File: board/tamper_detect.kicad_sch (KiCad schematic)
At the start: 12 parts

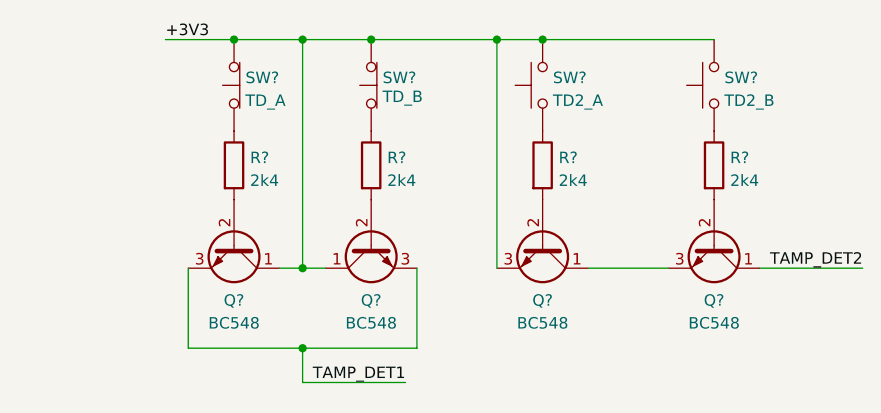
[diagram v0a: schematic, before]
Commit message: Add missing footprints.
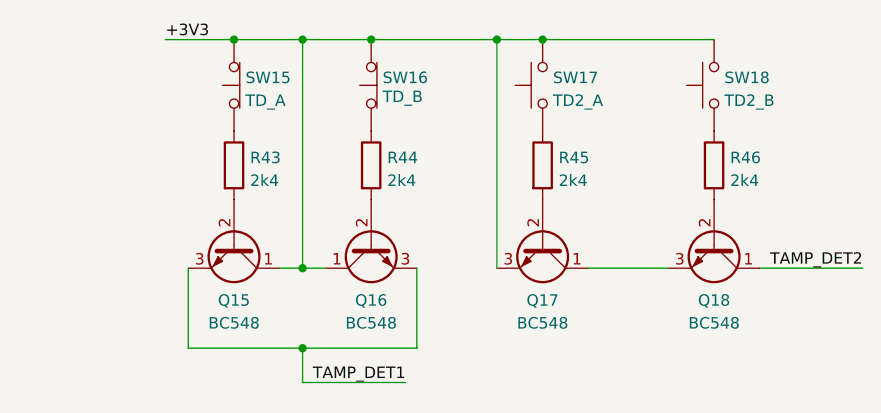
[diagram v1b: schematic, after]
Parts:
- R43, R44, R45, R46: renamed from R?; footprint (none) -> Resistor_THT:R_Axial_DIN0516_L15.5mm_D5.0mm_P7.62mm_Vertical
- SW15, SW16, SW17, SW18: renamed from SW?; footprint (none) -> Connector_Wire:SolderWire-1sqmm_1x02_P5.4mm_D1.4mm_OD2.7mm
- gave numbers to parts that had none: 4
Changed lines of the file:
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@@
   (symbol (lib_id "Device:R") (at 99.06 40.64 0) (unit 1)
     (in_bom yes) (on_board yes) (fields_autoplaced)
-    (property "Reference" "R?" (id 0) (at 100.838 39.8053 0)
+    (property "Reference" "R46" (id 0) (at 100.838 39.8053 0)
       (effects (font (size 1.27 1.27)) (justify left))
     )
@@
       (effects (font (size 1.27 1.27)) (justify left))
     )
-    (property "Footprint" "" (id 2) (at 97.282 40.64 90)
+    (property "Footprint" "Resistor_THT:R_Axial_DIN0516_L15.5mm_D5.0mm_P7.62mm_Vertical" (id 2) (at 97.282 40.64 90)
       (effects (font (size 1.27 1.27)) hide)
     )
@@
   (symbol (lib_id "Switch:SW_Push") (at 99.06 31.75 90) (unit 1)
     (in_bom yes) (on_board yes)
-    (property "Reference" "SW?" (id 0) (at 100.203 30.9153 90)
+    (property "Reference" "SW18" (id 0) (at 100.203 30.9153 90)
       (effects (font (size 1.27 1.27)) (justify right))
     )
@@
       (effects (font (size 1.27 1.27)) (justify right))
     )
-    (property "Footprint" "" (id 2) (at 93.98 31.75 0)
+    (property "Footprint" "Connector_Wire:SolderWire-1sqmm_1x02_P5.4mm_D1.4mm_OD2.7mm" (id 2) (at 93.98 31.75 0)
       (effects (font (size 1.27 1.27)) hide)
     )
@@
   (symbol (lib_id "Transistor_BJT:BC548") (at 80.01 49.53 270) (unit 1)
     (in_bom yes) (on_board yes) (fields_autoplaced)
-    (property "Reference" "Q?" (id 0) (at 80.01 55.6498 90))
+    (property "Reference" "Q17" (id 0) (at 80.01 55.6498 90))
     (property "Value" "BC548" (id 1) (at 80.01 58.1867 90))
     (property "Footprint" "Package_TO_SOT_THT:TO-92_Inline" (id 2) (at 78.105 54.61 0)
@@
   (symbol (lib_id "Device:R") (at 60.96 40.64 0) (unit 1)
     (in_bom yes) (on_board yes) (fields_autoplaced)
-    (property "Reference" "R?" (id 0) (at 62.738 39.8053 0)
+    (property "Reference" "R44" (id 0) (at 62.738 39.8053 0)
       (effects (font (size 1.27 1.27)) (justify left))
     )
@@
       (effects (font (size 1.27 1.27)) (justify left))
     )
-    (property "Footprint" "" (id 2) (at 59.182 40.64 90)
+    (property "Footprint" "Resistor_THT:R_Axial_DIN0516_L15.5mm_D5.0mm_P7.62mm_Vertical" (id 2) (at 59.182 40.64 90)
       (effects (font (size 1.27 1.27)) hide)
     )
@@
   (symbol (lib_id "Switch:SW_Push_Open") (at 45.72 31.75 90) (unit 1)
     (in_bom yes) (on_board yes) (fields_autoplaced)
-    (property "Reference" "SW?" (id 0) (at 46.99 30.9153 90)
+    (property "Reference" "SW15" (id 0) (at 46.99 30.9153 90)
       (effects (font (size 1.27 1.27)) (justify right))
     )
@@
       (effects (font (size 1.27 1.27)) (justify right))
     )
-    (property "Footprint" "" (id 2) (at 40.64 31.75 0)
+    (property "Footprint" "Connector_Wire:SolderWire-1sqmm_1x02_P5.4mm_D1.4mm_OD2.7mm" (id 2) (at 40.64 31.75 0)
       (effects (font (size 1.27 1.27)) hide)
     )
@@
   (symbol (lib_id "Transistor_BJT:BC548") (at 45.72 49.53 270) (unit 1)
     (in_bom yes) (on_board yes) (fields_autoplaced)
-    (property "Reference" "Q?" (id 0) (at 45.72 55.6498 90))
+    (property "Reference" "Q15" (id 0) (at 45.72 55.6498 90))
     (property "Value" "BC548" (id 1) (at 45.72 58.1867 90))
     (property "Footprint" "Package_TO_SOT_THT:TO-92_Inline" (id 2) (at 43.815 54.61 0)
@@
   (symbol (lib_id "Switch:SW_Push") (at 80.01 31.75 90) (unit 1)
     (in_bom yes) (on_board yes)
-    (property "Reference" "SW?" (id 0) (at 81.153 30.9153 90)
+    (property "Reference" "SW17" (id 0) (at 81.153 30.9153 90)
       (effects (font (size 1.27 1.27)) (justify right))
     )
@@
       (effects (font (size 1.27 1.27)) (justify right))
     )
-    (property "Footprint" "" (id 2) (at 74.93 31.75 0)
+    (property "Footprint" "Connector_Wire:SolderWire-1sqmm_1x02_P5.4mm_D1.4mm_OD2.7mm" (id 2) (at 74.93 31.75 0)
       (effects (font (size 1.27 1.27)) hide)
     )
@@
   (symbol (lib_id "Transistor_BJT:BC548") (at 99.06 49.53 270) (unit 1)
     (in_bom yes) (on_board yes) (fields_autoplaced)
-    (property "Reference" "Q?" (id 0) (at 99.06 55.6498 90))
+    (property "Reference" "Q18" (id 0) (at 99.06 55.6498 90))
     (property "Value" "BC548" (id 1) (at 99.06 58.1867 90))
     (property "Footprint" "Package_TO_SOT_THT:TO-92_Inline" (id 2) (at 97.155 54.61 0)
@@
   (symbol (lib_id "Device:R") (at 45.72 40.64 0) (unit 1)
     (in_bom yes) (on_board yes) (fields_autoplaced)
-    (property "Reference" "R?" (id 0) (at 47.498 39.8053 0)
+    (property "Reference" "R43" (id 0) (at 47.498 39.8053 0)
       (effects (font (size 1.27 1.27)) (justify left))
     )
@@
       (effects (font (size 1.27 1.27)) (justify left))
     )
-    (property "Footprint" "" (id 2) (at 43.942 40.64 90)
+    (property "Footprint" "Resistor_THT:R_Axial_DIN0516_L15.5mm_D5.0mm_P7.62mm_Vertical" (id 2) (at 43.942 40.64 90)
       (effects (font (size 1.27 1.27)) hide)
     )
@@
   (symbol (lib_id "Device:R") (at 80.01 40.64 0) (unit 1)
     (in_bom yes) (on_board yes) (fields_autoplaced)
-    (property "Reference" "R?" (id 0) (at 81.788 39.8053 0)
+    (property "Reference" "R45" (id 0) (at 81.788 39.8053 0)
       (effects (font (size 1.27 1.27)) (justify left))
     )
@@
       (effects (font (size 1.27 1.27)) (justify left))
     )
-    (property "Footprint" "" (id 2) (at 78.232 40.64 90)
+    (property "Footprint" "Resistor_THT:R_Axial_DIN0516_L15.5mm_D5.0mm_P7.62mm_Vertical" (id 2) (at 78.232 40.64 90)
       (effects (font (size 1.27 1.27)) hide)
     )
@@
   (symbol (lib_id "Transistor_BJT:BC548") (at 60.96 49.53 90) (mirror x) (unit 1)
     (in_bom yes) (on_board yes) (fields_autoplaced)
-    (property "Reference" "Q?" (id 0) (at 60.96 55.6498 90))
+    (property "Reference" "Q16" (id 0) (at 60.96 55.6498 90))
     (property "Value" "BC548" (id 1) (at 60.96 58.1867 90))
     (property "Footprint" "Package_TO_SOT_THT:TO-92_Inline" (id 2) (at 62.865 54.61 0)
@@
   (symbol (lib_id "Switch:SW_Push_Open") (at 60.96 31.75 90) (unit 1)
     (in_bom yes) (on_board yes)
-    (property "Reference" "SW?" (id 0) (at 62.23 30.9153 90)
+    (property "Reference" "SW16" (id 0) (at 62.23 30.9153 90)
       (effects (font (size 1.27 1.27)) (justify right))
     )
@@
       (effects (font (size 1.27 1.27)) (justify right))
     )
-    (property "Footprint" "" (id 2) (at 55.88 31.75 0)
+    (property "Footprint" "Connector_Wire:SolderWire-1sqmm_1x02_P5.4mm_D1.4mm_OD2.7mm" (id 2) (at 55.88 31.75 0)
       (effects (font (size 1.27 1.27)) hide)
     )

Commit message: Change net descriptors.
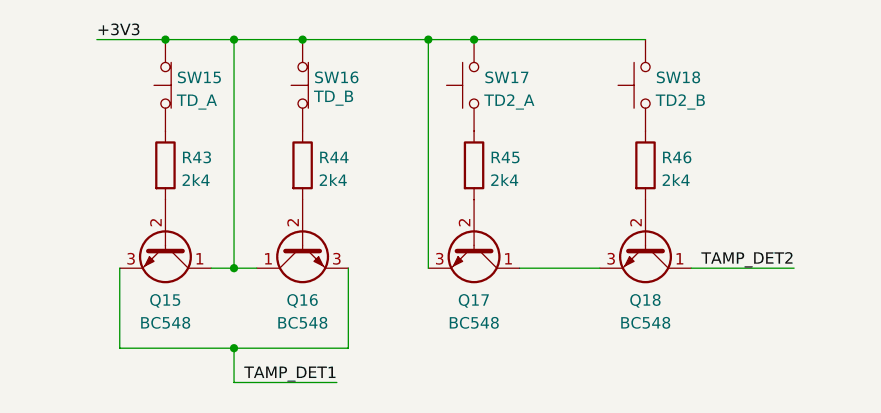
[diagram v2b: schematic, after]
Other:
- moved on the sheet: Q15, Q16, Q17, Q18, R43, R44, R45, R46, SW15, SW16, SW17, SW18

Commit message: Make it a multiboard project.
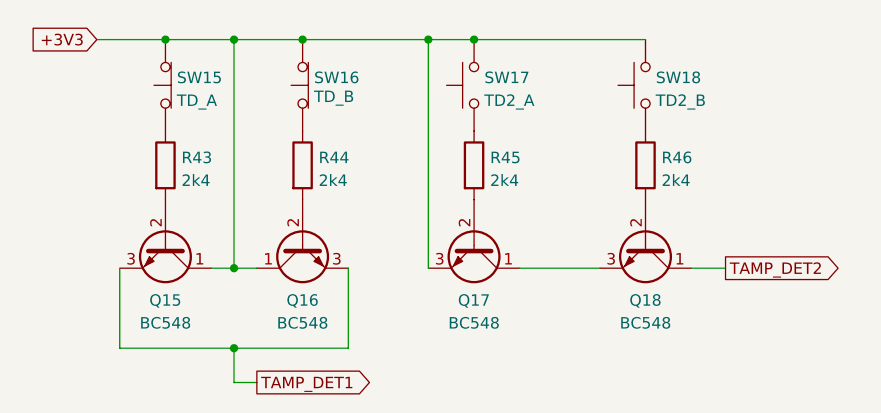
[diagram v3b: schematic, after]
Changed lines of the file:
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@@
     (stroke (width 0) (type default) (color 0 0 0 0))
   )
-  (wire (pts (xy 96.52 52.07) (xy 107.95 52.07))
+  (wire (pts (xy 96.52 52.07) (xy 100.33 52.07))
     (stroke (width 0) (type default) (color 0 0 0 0))
   )
@@
     (stroke (width 0) (type default) (color 0 0 0 0))
   )
-  (wire (pts (xy 57.15 64.77) (xy 45.72 64.77))
+  (wire (pts (xy 48.26 64.77) (xy 45.72 64.77))
     (stroke (width 0) (type default) (color 0 0 0 0))
   )
-  (label "TAMP_DET2" (at 107.95 52.07 180)
-    (effects (font (size 1.27 1.27)) (justify right bottom))
+  (global_label "TAMP_DET2" (shape output) (at 100.33 52.07 0) (fields_autoplaced)
+    (effects (font (size 1.27 1.27)) (justify left))
+    (property "Referenzen zwischen Schaltplänen" "${INTERSHEET_REFS}" (id 0) (at 113.275 51.9906 0)
+      (effects (font (size 1.27 1.27)) (justify left) hide)
+    )
   )
-  (label "TAMP_DET1" (at 57.15 64.77 180)
-    (effects (font (size 1.27 1.27)) (justify right bottom))
+  (global_label "TAMP_DET1" (shape output) (at 48.26 64.77 0) (fields_autoplaced)
+    (effects (font (size 1.27 1.27)) (justify left))
+    (property "Referenzen zwischen Schaltplänen" "${INTERSHEET_REFS}" (id 0) (at 61.205 64.6906 0)
+      (effects (font (size 1.27 1.27)) (justify left) hide)
+    )
   )
-  (label "+3V3" (at 30.48 26.67 0)
-    (effects (font (size 1.27 1.27)) (justify left bottom))
+  (global_label "+3V3" (shape input) (at 30.48 26.67 180) (fields_autoplaced)
+    (effects (font (size 1.27 1.27)) (justify right))
+    (property "Referenzen zwischen Schaltplänen" "${INTERSHEET_REFS}" (id 0) (at 22.7964 26.5906 0)
+      (effects (font (size 1.27 1.27)) (justify right) hide)
+    )
   )
   (symbol (lib_id "Device:R") (at 91.44 40.64 0) (unit 1)
